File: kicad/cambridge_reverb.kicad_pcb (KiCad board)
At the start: 2 copper layers, 190 x 115 mm, 102 parts, among them IC1 TL072CP, IC2 TL072CP, Q1 MMBF5457, Q2 MMBF5457, T1 reuse / AnTek AS-0524, U1 LM317T

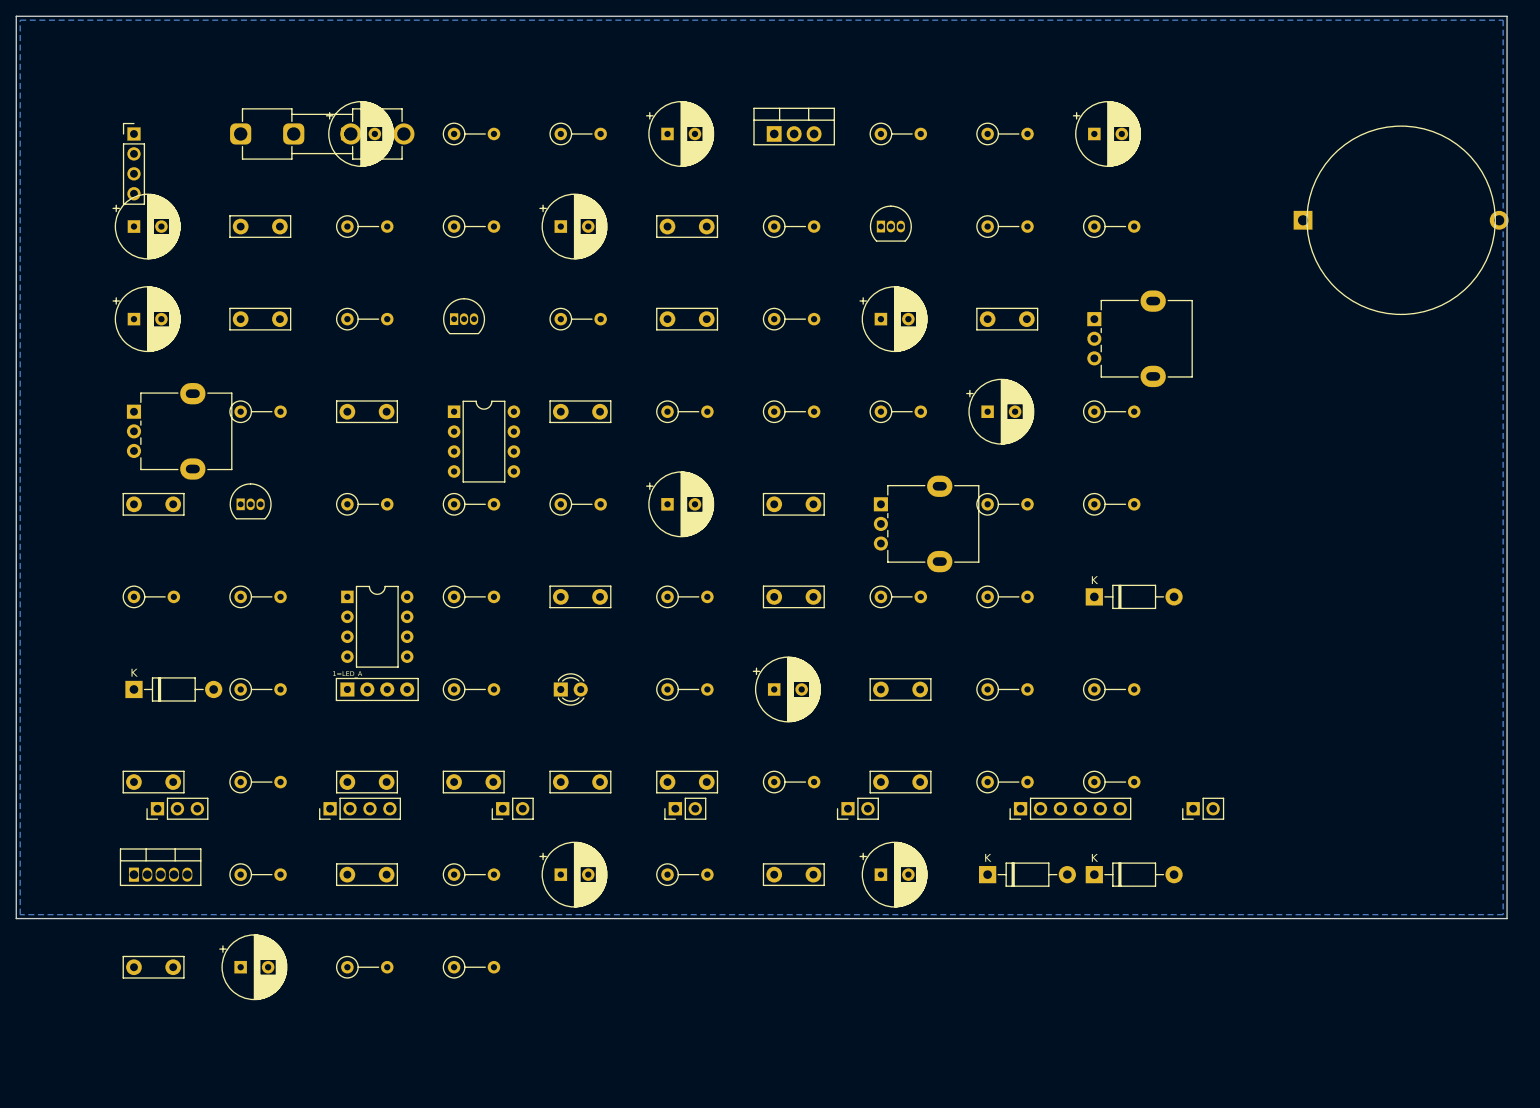
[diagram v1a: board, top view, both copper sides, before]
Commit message: Audit pass: center schematic pages, PCB layout audit, SPICE audit
Schematic: gen_kicad.py now defers draw-op emission, computes each sheet's
content bounding box, and translates it to the page center (grid-snapped so pins
stay on the 1.27mm grid). All 8 sheets are centered on the page instead of
crammed top-left; ERC still 0 violations.

PCB: full category-by-category audit in kicad/PCB-AUDIT.md (footprints,
placement, net classes, copper/GND, routing) with prioritized fixes. Applied:
- the 5 reused/off-board pots were modeled with a 16mm panel-pot footprint; they
  are panel-mounted (wired off-board), so they're now 3-pad wiring connectors --
  more correct and a big silk-overlap source removed (packing 51%->48%)
- centered the component grid
Documented findings: LM1875 TO-220-5 annular is 0.0875mm (1.275mm pad on 1.1mm
drill) vs the 0.15mm rule; KBP410G bridge uses a placeholder header footprint;
silk/courtyard overlaps are a density symptom (the 82% packing on the 155x90
safe-bet). Non-routing DRC errors: 9; demo board still 0.

SPICE: audited every netlist/model (spice/README.md). All five run under
ngspice-42 (exit 0) and match the documented numbers; no correctness issues.

https://claude.ai/code/session_01PkrfUi9tvZfLvudJ7h23qD
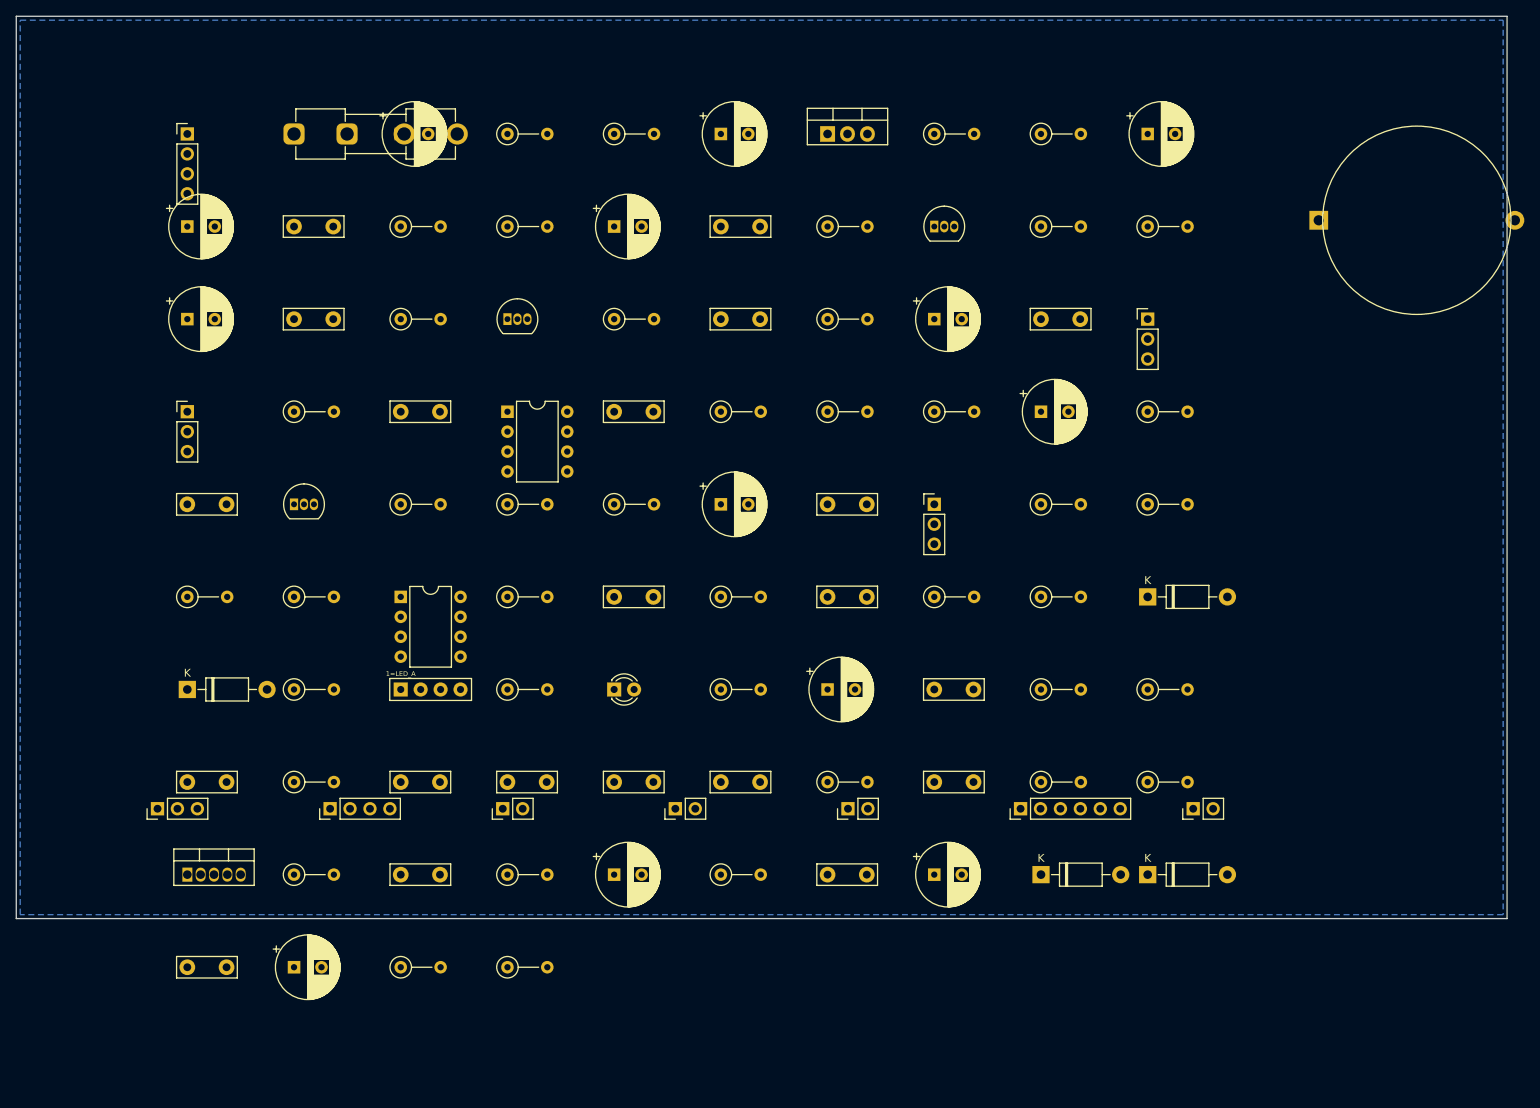
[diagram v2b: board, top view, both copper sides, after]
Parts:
- removed the POT_REV at (110.2, 62.2)
- removed the POT_TONE at (15.0, 50.4)
- removed the POT_VOL at (137.4, 38.6)
- added POT_REV: reuse, PinHeader_1x03_P2.54mm_Vertical, F.Cu at (117.0, 62.2)
- added POT_TONE: reuse, PinHeader_1x03_P2.54mm_Vertical, F.Cu at (21.8, 50.4)
- added POT_VOL: reuse, PinHeader_1x03_P2.54mm_Vertical, F.Cu at (144.2, 38.6)
- moved C_reg_in 6.80 mm to (144.2, 15.0)
- moved D2 6.80 mm to (144.2, 109.4)
- moved D_lfo1 6.80 mm to (144.2, 74.0)
- moved R_bias2 6.80 mm to (144.2, 97.6)
- moved R_blend2 6.80 mm to (144.2, 62.2)
- moved R_drv3 6.80 mm to (144.2, 50.4)
- moved R_fs_trem 6.80 mm to (144.2, 85.8)
- moved R_s1 6.80 mm to (144.2, 26.8)
- moved C_dc_blk 6.80 mm to (103.4, 85.8)
- moved C_lfo2 6.80 mm to (103.4, 74.0)
- moved C_rev4 6.80 mm to (103.4, 62.2)
- moved C_zobel 6.80 mm to (103.4, 109.4)
- moved R_drv1 6.80 mm to (103.4, 50.4)
- moved R_fs_mrb 6.80 mm to (103.4, 97.6)
- moved R_g1 6.80 mm to (103.4, 26.8)
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
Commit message: Keep LM317-input pre-filter (rename +27V->VREG_IN, 47R->100R) - corrected call
On reflection my earlier "delete R_27V, feed LM317 from +33.5V" recommendation
was wrong for a noise-conscious design: R_27V + C_filt1 is an RC pre-filter on
the LM317 input AND decouples the preamp supply from the power amp's transient
current draw on the +33.5V rail (the LM317's PSRR alone falls off with
frequency). Deleting it would hurt noise.

The real bug was the mislabeling: under the modern ~15 mA load the node sits at
~32 V, not 27 V, so the "27 V rail / 26-28 V" naming was a leftover misnomer.

Done instead:
- keep the element; bump 47R/2W -> 100R/1W (~6 dB more 120 Hz ripple rejection,
  ~1.5 V drop at 15 mA, LM317 in-out diff 14.7 V << 40 V max, ~0.02 W)
- rename net +27V -> VREG_IN (schematic gen, .kicad_pro Power pattern)
- correct the docs/troubleshooting voltages (~31-33 V) across Part 1/2/3/4,
  errata, BOM, availability-audit, PCB-NOTES/AUDIT, SCHEMATIC-BUILD, CHECKLIST

Verified: sch erc 0, full DRC unchanged (164), demo DRC 0, SPICE exit 0, BOM
CSV clean, net classes intact (VREG_IN now in the Power pattern).

https://claude.ai/code/session_01PkrfUi9tvZfLvudJ7h23qD
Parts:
- R_27V: value 47R/2W -> 100R/1W
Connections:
- net +27V renamed VREG_IN

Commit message: Roast pass (2026-06-16): fix missing mains fuse, correct 18W->~12W spec, +more
Adversarial review (docs/roast-2026-06-16.md), every finding verified by math or
file. Fixes applied:

R1 (SAFETY, was missing): added a MAINS PRIMARY fuse. The only fuse was a 1A on
   the secondary DC rail, which doesn't protect against a primary/transformer/
   bridge fault. Added T800mA/250V (120V; ~T400mA at 230V) to BOM + Part 1 safety
   + Part 3.
R2 (spec error I propagated last pass): "18 W into 8 ohm" is physically
   unreachable on a 33.5 V single rail -- needs 17.0 V peak, only 16.75 V exists.
   Real ceiling ~12 W clean (17.5 W absolute). Corrected Part 1 sec.3, Part 5
   thermal, and the component-availability-audit current/transformer numbers
   (which I'd built on the bad 18 W: ~30 VA min, not ~50 VA "match").
R3: the reverb dry/wet mixer is broken as drawn -- 1M series in the dry path vs
   220k wet made it ~all-wet, into an unbuffered high-Z blend node. Rebalanced
   R_dry_tap 1M->220k and flagged loudly that the inter-effect chain needs a real
   buffered summing stage before fab.
R4: marked the orphaned Wiring_Edge_Array_35 footprint (advertised, never placed)
   as unused/reference.
R5-R8 (documented): F1 sits in the C_main inrush path (prefer AC-secondary);
   shared VBIAS can bleed tremolo into reverb; "SPICE-verified" oversells (the
   macromodel is rail-less -> no single-supply headroom/clipping check); and the
   CHANGELOG was incoherent (floating section, all-same-date) -> consolidated.

Verified after regen: sch erc 0, full DRC unchanged (164), demo DRC 0, SPICE
exit 0, BOM CSV clean.

https://claude.ai/code/session_01PkrfUi9tvZfLvudJ7h23qD
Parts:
- R_dry_tap: value 1M -> 220k

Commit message: Redesign effects chain: active reverb summer + output buffer + split bias
Resolves roast R3 (broken passive mixer) and R6 (shared VBIAS bleed), using the
two spare TL072 halves and verifying with a rail-aware SPICE model.

- Reverb wet/dry mix is now an ACTIVE inverting summer on IC1-B (dry always on,
  wet via POT_REV, unity each, low-Z out about VBIAS_R). Removed the broken
  passive R_dry_tap/R_blend1/R_blend2 (1M dry series made it ~all-wet into an
  unbuffered 110k node).
- IC2-B repurposed as the post-MRB OUTPUT BUFFER driving PA_IN (removed the
  unbuffered R_painput 1M and a dead C_trem_out/R_trem_pass branch).
- VBIAS split into independent VBIAS_R (reverb) and VBIAS_T (tremolo) dividers
  (100k/100k + 47uF each) -> the LFO can no longer modulate the reverb reference.

Verification: new models/opamp_rail.sub clamps the output to the rails (unlike
opamp1p.sub), and spice/tran_reverb_mixer.cir confirms on a single +17V supply:
mid-rail bias 8.50 V, unity (0.0 dB) sum, clips at 15.5/1.5 V -> +-7 V headroom
(~24 dB over a 0.42 V program peak). This is the large-signal/headroom check the
rail-less model could not do (roast R7).

ERC 0; demo DRC 0; full board regenerated (106 footprints); run_all.sh exit 0;
BOM + roast doc + SCHEMATIC-BUILD + spice/README + CHANGELOG updated.

https://claude.ai/code/session_01PkrfUi9tvZfLvudJ7h23qD
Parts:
- removed C_trem_out: 100nF, C_Disc_D7.5mm_W2.5mm_P5.00mm
- removed C_vb: 10uF/25V, CP_Radial_D8.0mm_P3.50mm
- removed R_blend1, R_blend2, R_dry_tap: 220k, R_Axial_DIN0207_L6.3mm_D2.5mm_P5.08mm_Vertical
- removed R_painput, R_trem_pass: 1M, R_Axial_DIN0207_L6.3mm_D2.5mm_P5.08mm_Vertical
- removed R_vb1, R_vb2: 100k, R_Axial_DIN0207_L6.3mm_D2.5mm_P5.08mm_Vertical
- added C_drymix: 1uF, C_Disc_D7.5mm_W2.5mm_P5.00mm, F.Cu at (49.0, 74.0)
- added C_obuf_in: 1uF, C_Disc_D7.5mm_W2.5mm_P5.00mm, F.Cu at (130.6, 74.0)
- added C_vbr: 47uF/25V, CP_Radial_D8.0mm_P3.50mm, F.Cu at (76.2, 26.8)
- added C_vbt: 47uF/25V, CP_Radial_D8.0mm_P3.50mm, F.Cu at (117.0, 26.8)
- added C_wetmix: 1uF, C_Disc_D7.5mm_W2.5mm_P5.00mm, F.Cu at (76.2, 74.0)
- added R_drymix: 100k, R_Axial_DIN0207_L6.3mm_D2.5mm_P5.08mm_Vertical, F.Cu at (62.6, 74.0)
- added R_mixfb: 100k, R_Axial_DIN0207_L6.3mm_D2.5mm_P5.08mm_Vertical, F.Cu at (35.4, 74.0)
- added R_obuf_b: 100k, R_Axial_DIN0207_L6.3mm_D2.5mm_P5.08mm_Vertical, F.Cu at (144.2, 74.0)
- added R_vbr1: 100k, R_Axial_DIN0207_L6.3mm_D2.5mm_P5.08mm_Vertical, F.Cu at (49.0, 26.8)
- added R_vbr2: 100k, R_Axial_DIN0207_L6.3mm_D2.5mm_P5.08mm_Vertical, F.Cu at (62.6, 26.8)
- added R_vbt1: 100k, R_Axial_DIN0207_L6.3mm_D2.5mm_P5.08mm_Vertical, F.Cu at (89.8, 26.8)
- added R_vbt2: 100k, R_Axial_DIN0207_L6.3mm_D2.5mm_P5.08mm_Vertical, F.Cu at (103.4, 26.8)
- added R_wetmix: 100k, R_Axial_DIN0207_L6.3mm_D2.5mm_P5.08mm_Vertical, F.Cu at (89.8, 74.0)
- moved C_s2 95.9 mm to (21.8, 50.4)
- moved POT_REV 95.9 mm to (21.8, 74.0)
- moved Q1 95.9 mm to (21.8, 38.6)
- moved R_drv2 95.9 mm to (21.8, 62.2)
- moved C_rev1 95.9 mm to (35.4, 62.2)
- moved C_treble 95.9 mm to (35.4, 50.4)
- moved POT_VOL 95.9 mm to (49.0, 50.4)
- moved R_d1 95.9 mm to (35.4, 38.6)
- moved R_drv3 95.9 mm to (49.0, 62.2)
- moved R_s1 95.9 mm to (49.0, 38.6)
- moved D_lfo2 95.2 mm to (117.0, 85.8)
- moved R_led 95.2 mm to (130.6, 85.8)
- moved VTL1 95.2 mm to (144.2, 85.8)
- moved C_in_pa 69.0 mm to (49.0, 109.4)
- moved C_mrb_out 69.0 mm to (21.8, 109.4)
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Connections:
- C_lfo2 pad 2: VBIAS -> VBIAS_T
- IC1 pad 5: VBIAS -> VBIAS_R
- IC1 pad 6: SP1N -> SUMJ
- IC1 pad 7: SP1N -> BLEND
- IC2 pad 5: VBIAS -> OBUF_IN
- IC2 pad 6: SP2N -> PA_IN
- IC2 pad 7: SP2N -> PA_IN
- R_drv2 pad 2: VBIAS -> VBIAS_R
- R_drvbias pad 2: VBIAS -> VBIAS_R
- R_lfo1 pad 2: VBIAS -> VBIAS_T
- R_lfo_fb2 pad 2: VBIAS -> VBIAS_T

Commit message: Generate BOM from schematic (authoritative); complete missing schematic parts
The BOM had drifted badly from the schematic (~20 parts in the schematic missing
from the BOM, ~20 stale/renamed rows in the BOM). Root-caused two ways:

1. Completed the SCHEMATIC -- added parts that were in Part 2 / the BOM but never
   actually placed: rectifier snubbers C101-C104, 2nd pre-filter C_filt2, and the
   tremolo SPEED/DEPTH pots (POT_SPD as a rheostat in the Wien series arm to vary
   frequency; POT_DPT scaling the LFO into the VTL1 LED for depth). 117 comps, ERC 0.

2. Made the BOM GENERATED from the schematic: kicad/gen/gen_bom.py emits bom/bom.csv
   per-reference 1:1 with the netlist (verified: every schematic ref present),
   merged with curated part numbers/notes and an explicit off-board/mechanical
   section (sockets, heatsink, mica, standoffs, fuses, mains fuse). Also writes
   bom/bom-grouped.csv (consolidated by value+footprint for ordering). bom/README
   updated to say it's generated; do not hand-edit.

Verified: sch erc 0, demo DRC 0, run_all.sh exit 0, BOM 8-col clean, every
schematic ref covered. Full board now 113 footprints; density 53%/90% (190x115 /
155x90) -- reinforces the chassis-fit finding.

https://claude.ai/code/session_01PkrfUi9tvZfLvudJ7h23qD
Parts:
- added C101: 10nF/100V, C_Disc_D7.5mm_W2.5mm_P5.00mm, F.Cu at (76.2, 15.0)
- added C102: 10nF/100V, C_Disc_D7.5mm_W2.5mm_P5.00mm, F.Cu at (89.8, 15.0)
- added C103: 10nF/100V, C_Disc_D7.5mm_W2.5mm_P5.00mm, F.Cu at (103.4, 15.0)
- added C104: 10nF/100V, C_Disc_D7.5mm_W2.5mm_P5.00mm, F.Cu at (117.0, 15.0)
- added C_filt2: 1000uF/50V, CP_Radial_D8.0mm_P3.50mm, F.Cu at (21.8, 26.8)
- added POT_DPT: 100k lin, PinHeader_1x03_P2.54mm_Vertical, F.Cu at (76.2, 97.6)
- added POT_SPD: 500k lin, PinHeader_1x03_P2.54mm_Vertical, F.Cu at (103.4, 85.8)
- R_lfo_ser: value 100k -> 10k
- moved C_mrb_out 95.2 mm to (117.0, 109.4)
- moved R_led_diag 95.2 mm to (117.0, 97.6)
- moved R_zobel 95.2 mm to (117.0, 121.2)
- moved C_in_pa 95.2 mm to (144.2, 109.4)
- moved C_out 95.2 mm to (144.2, 121.2)
- moved C_zobel 95.2 mm to (130.6, 121.2)
- moved LED_rate 95.2 mm to (130.6, 97.6)
- moved R_fs_mrb 95.2 mm to (130.6, 109.4)
- moved R_trem1 95.2 mm to (144.2, 97.6)
- moved C_lfo1 81.6 mm to (117.0, 85.8)
- moved C_lfo2 81.6 mm to (144.2, 85.8)
- moved R_lfo1 81.6 mm to (130.6, 85.8)
- moved C_drvin 69.0 mm to (49.0, 62.2)
- moved C_in_pre 69.0 mm to (62.6, 38.6)
- moved C_obuf_in 69.0 mm to (62.6, 85.8)
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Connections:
- R_led pad 1: LFO_OUT -> DPT_W
- R_lfo_ser pad 2: WN1 -> SPD_A

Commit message: Design + verify the tone stack (Vox treble-cut substitute)
The tone sheet was a TBD placeholder (original 25-5274-2 values never recovered).
Replaced with a working passive Vox-style control: Volume pot + a treble "cut"
(C_cut 10nF + POT_TONE 100k to ground). Verified in spice/ac_tonestack.cir:
flat at bright (-1.6 dB, just insertion loss), musical treble cut at the dark end
(-9 dB @ 5 kHz, -14 dB @ 10 kHz). Clearly flagged as a designed substitute (the
original panel may have had separate Treble/Bass) in the sheet note, cross-check
#4, and spice/README.

All 7 ngspice blocks now pass (added ac_tonestack.cir). ERC 0, demo DRC 0, BOM
regenerated from the schematic (no TBD rows left).

https://claude.ai/code/session_01PkrfUi9tvZfLvudJ7h23qD
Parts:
- removed C_tone_tbd: TBD, C_Disc_D7.5mm_W2.5mm_P5.00mm
- added C_cut: 10nF, C_Disc_D7.5mm_W2.5mm_P5.00mm, F.Cu at (144.2, 50.4)
- POT_TONE: value reuse -> 100k lin
- POT_VOL: value reuse -> 250k log
- moved POT_TONE 109.4 mm to (21.8, 62.2)
- moved R_fx_pad 13.6 mm to (130.6, 50.4)
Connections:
- POT_TONE pad 1: VOL_W -> TCW
- POT_TONE pad 2: TONE_OUT -> GND
- POT_VOL pad 2: VOL_W -> TONE_OUT
- R_fx_pad pad 1: VOL_W -> TONE_OUT

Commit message: Normalize BOM value strings; refresh stale top-level README
- gen_kicad NV(): normalize value strings for a tidy/consolidated BOM (2K2->2.2k,
  4K7->4.7k, drop the " film" descriptor that the footprint already conveys).
  Cosmetic only; ERC 0, demo DRC 0, SPICE exit 0, BOM regenerated.
- README rewritten to reflect the actual current state instead of the original
  reconstructed-docs snapshot: the generated + tool-verified KiCad/BOM/ngspice
  flow, the verified ~12 W power ceiling (not 18 W), the required mains fuse, the
  190x115 board + chassis-fit caveat, the active effects-chain/tone redesigns,
  and the provenance/honesty framing.

https://claude.ai/code/session_01PkrfUi9tvZfLvudJ7h23qD
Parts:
- C_in_pa: value 1uF film -> 1uF
- R_led_diag, R_rec2, R_s1, R_s2: value 2K2 -> 2.2k
- R_lfo_fb2: value 4K7 -> 4.7k
